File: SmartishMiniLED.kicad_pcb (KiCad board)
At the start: 2 copper layers, 24.9 x 55.4 mm, 35 parts, among them J1 USB_C_Receptacle_USB2.0, J2 BUTTON, J3 Screw_Terminal_01x03, P1 NeopixelStripPads, P2 NeopixelStripPads, Q1 MMBT2222, Q2 MMBT2222, Q3 IRLML6344, Q4 IRF7410, SW2 TL3342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

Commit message: 2nd attempt to fix DRC errors
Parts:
- AE1: footprint RF_Antenna:Texas_SWRA117D_2.4GHz_Right -> SmartishMiniLED:Texas_SWRA117D_2.4GHz_Right
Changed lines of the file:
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@@
     (pad "" np_thru_hole circle (at 0 0) (size 3.2 3.2) (drill 3.2) (layers *.Cu *.Mask))
   )
-  (footprint "RF_Antenna:Texas_SWRA117D_2.4GHz_Right" (layer "F.Cu")
+  (footprint "SmartishMiniLED:Texas_SWRA117D_2.4GHz_Right" (layer "F.Cu")
     (at 155.956 92.964 -90)
     (descr "http://www.ti.com/lit/an/swra117d/swra117d.pdf")
-    (tags "PCB antenna")
+    (tags "net tie PCB antenna")
     (property "Sheetfile" "SmartishMiniLED.kicad_sch")
     (property "Sheetname" "")
@@
         (xy 2.45 -2.51)
       ) (layer "F.Cu") (width 0) (fill solid))
+    (fp_line (start -3.05 -5.45) (end 12.15 -0.25) (layer "Dwgs.User") (width 0.15))
+    (fp_line (start -3.05 -5.45) (end 12.15 -5.45) (layer "Dwgs.User") (width 0.15))
+    (fp_line (start 12.15 -0.25) (end 12.15 -5.45) (layer "Dwgs.User") (width 0.15))
+    (fp_line (start -3.05 -0.25) (end -3.05 -5.45) (layer "Dwgs.User") (width 0.15))
+    (fp_line (start -3.05 -0.25) (end 12.15 -5.45) (layer "Dwgs.User") (width 0.15))
     (fp_line (start -3.05 -0.25) (end 12.15 -0.25) (layer "Dwgs.User") (width 0.15))
-    (fp_line (start 12.15 -0.25) (end 12.15 -5.45) (layer "Dwgs.User") (width 0.15))
-    (fp_line (start -3.05 -0.25) (end 12.15 -5.45) (layer "Dwgs.User") (width 0.15))
-    (fp_line (start -3.05 -5.45) (end 12.15 -5.45) (layer "Dwgs.User") (width 0.15))
-    (fp_line (start -3.05 -5.45) (end 12.15 -0.25) (layer "Dwgs.User") (width 0.15))
-    (fp_line (start -3.05 -0.25) (end -3.05 -5.45) (layer "Dwgs.User") (width 0.15))
+    (fp_line (start -3.2 -5.6) (end 12.3 -5.6) (layer "F.CrtYd") (width 0.05))
+    (fp_line (start -3.2 0.35) (end -3.2 -5.6) (layer "F.CrtYd") (width 0.05))
+    (fp_line (start 12.3 0.35) (end -3.2 0.35) (layer "F.CrtYd") (width 0.05))
     (fp_line (start 12.3 -5.6) (end 12.3 0.35) (layer "F.CrtYd") (width 0.05))
-    (fp_line (start -3.2 -5.6) (end 12.3 -5.6) (layer "F.CrtYd") (width 0.05))
-    (fp_line (start 12.3 0.35) (end -3.2 0.35) (layer "F.CrtYd") (width 0.05))
-    (fp_line (start -3.2 0.35) (end -3.2 -5.6) (layer "F.CrtYd") (width 0.05))
-    (fp_line (start -3.2 0.35) (end -3.2 -5.6) (layer "F.Fab") (width 0.15))
     (fp_line (start -3.2 -5.6) (end 12.3 -5.6) (layer "F.Fab") (width 0.15))
     (fp_line (start 12.3 -5.6) (end 12.3 0.35) (layer "F.Fab") (width 0.15))
+    (fp_line (start -3.2 0.35) (end -3.2 -5.6) (layer "F.Fab") (width 0.15))
     (fp_line (start 12.3 0.35) (end -3.2 0.35) (layer "F.Fab") (width 0.15))
     (pad "1" connect rect (at 0 0 270) (size 0.5 0.5) (layers "F.Cu")

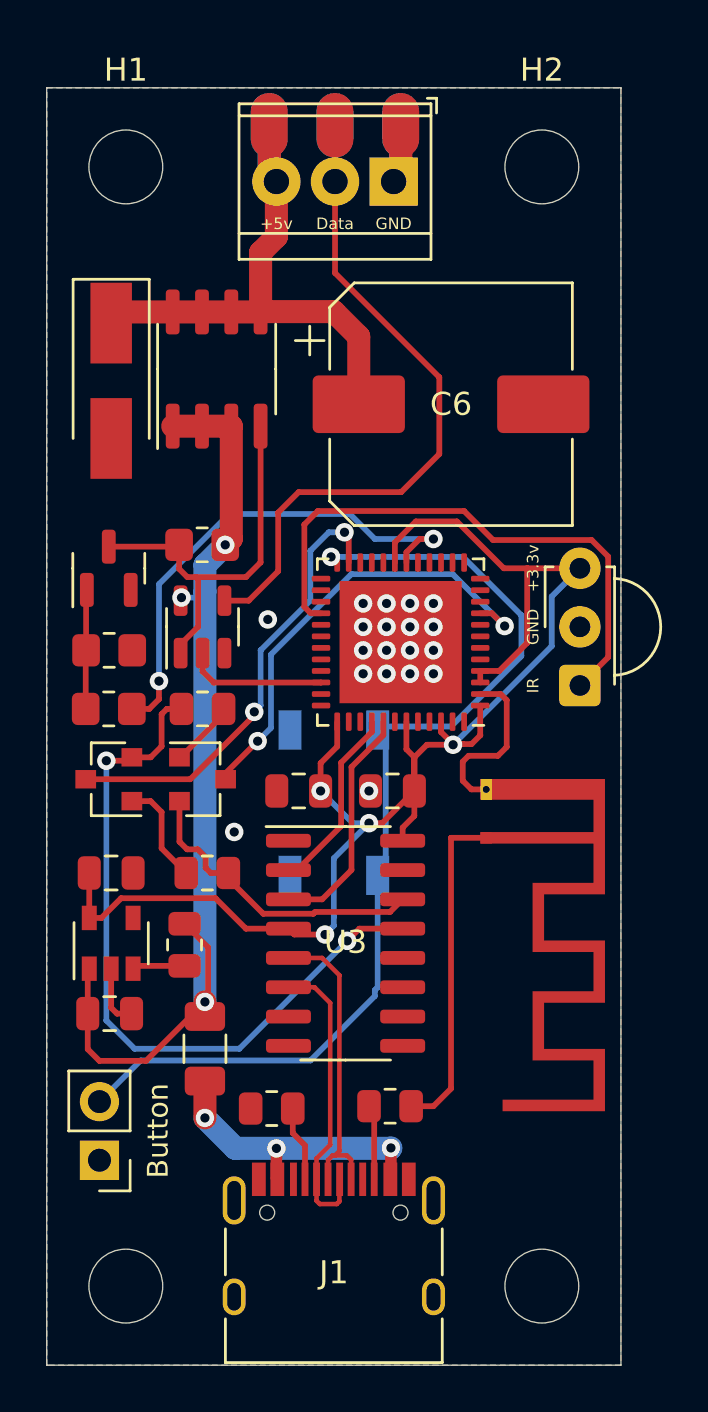
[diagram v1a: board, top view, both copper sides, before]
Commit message: Increased main power line to 1.5mm, should handle 3A
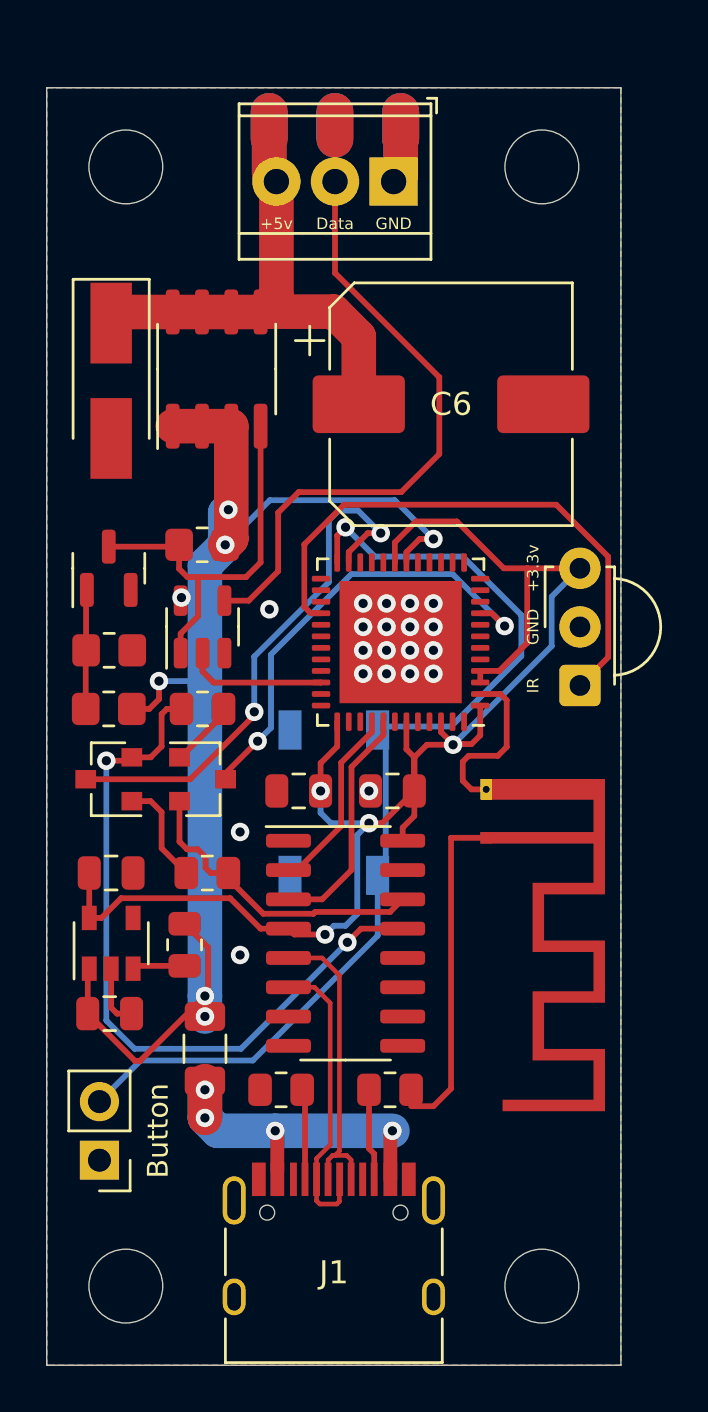
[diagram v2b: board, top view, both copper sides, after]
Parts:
- moved R6 0.91 mm to (147.1, 103.9)
- moved R5 0.71 mm to (151.8, 103.9)
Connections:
- R7 pad 2: /LED_POWER -> +5V
- U1 pad 18: /LED_POWER -> +5V
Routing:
- net /LED_POWER: track 21.8 -> 0.00 mm, vias 2 -> 0
- net +5V: track 43.7 -> 61.1 mm, vias 3 -> 7
- net /GPIO0: track 19.8 -> 23.2 mm
- net Net-(F1-Pad1): track 12.9 -> 15.4 mm, vias 3 -> 4
- net +3V3: track 66.7 -> 67.6 mm
- net GND: vias 19 -> 20

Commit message: Added some id text
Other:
- board text added: "Smartish MiniLED"
- board text added: "v1.0"
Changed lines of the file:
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@@
   )
   (gr_rect (start 161.798 115.824) (end 136.906 60.452) (layer "Edge.Cuts") (width 0.05) (fill none))
+  (gr_text "v1.0" (at 149.606 72.39) (layer "B.Cu")
+    (effects (font (size 1 1) (thickness 0.2)) (justify mirror))
+  )
   (gr_text "+5v" (at 146.83899 66.548) (layer "B.SilkS")
     (effects (font (size 0.5 0.5) (thickness 0.125)) (justify mirror))
@@
     (effects (font (size 0.5 0.5) (thickness 0.125)) (justify mirror))
   )
+  (gr_text "Smartish MiniLED" (at 149.352 70.104) (layer "B.SilkS")
+    (effects (font (size 1.5 1.5) (thickness 0.3) italic) (justify mirror))
+  )
   (gr_text "Data" (at 149.37899 66.548) (layer "B.SilkS")

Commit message: A few fixes and tidy ups
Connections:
- R7 pad 2: +5V -> /LED_POWER
- U1 pad 18: +5V -> /LED_POWER
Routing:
- net /LED_POWER: track 0.00 -> 24.2 mm, vias 0 -> 2
- net +5V: track 61.1 -> 44.5 mm, vias 7 -> 5
- net GND: track 23.1 -> 9.31 mm
- net /GPIO0: track 23.2 -> 21.1 mm
- net Net-(AE1-Pad2): track 7.45 -> 5.74 mm
- net /IR: track 24.5 -> 25.6 mm
- net /DATA_OUT: track 32.0 -> 32.9 mm
